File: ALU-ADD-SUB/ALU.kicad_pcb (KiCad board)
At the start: 4 copper layers, 122.2 x 30.8 mm, 26 parts, among them J1 Conn_01x02, J2 Conn_01x08, J3 Conn_01x08, J4 Conn_01x08, J5 Conn_01x02, J6 Conn_01x08, J8 Conn_01x02, U11 74LS245, U12 74LS283, U13 74LS283, U14 74LS86, U15 74LS86

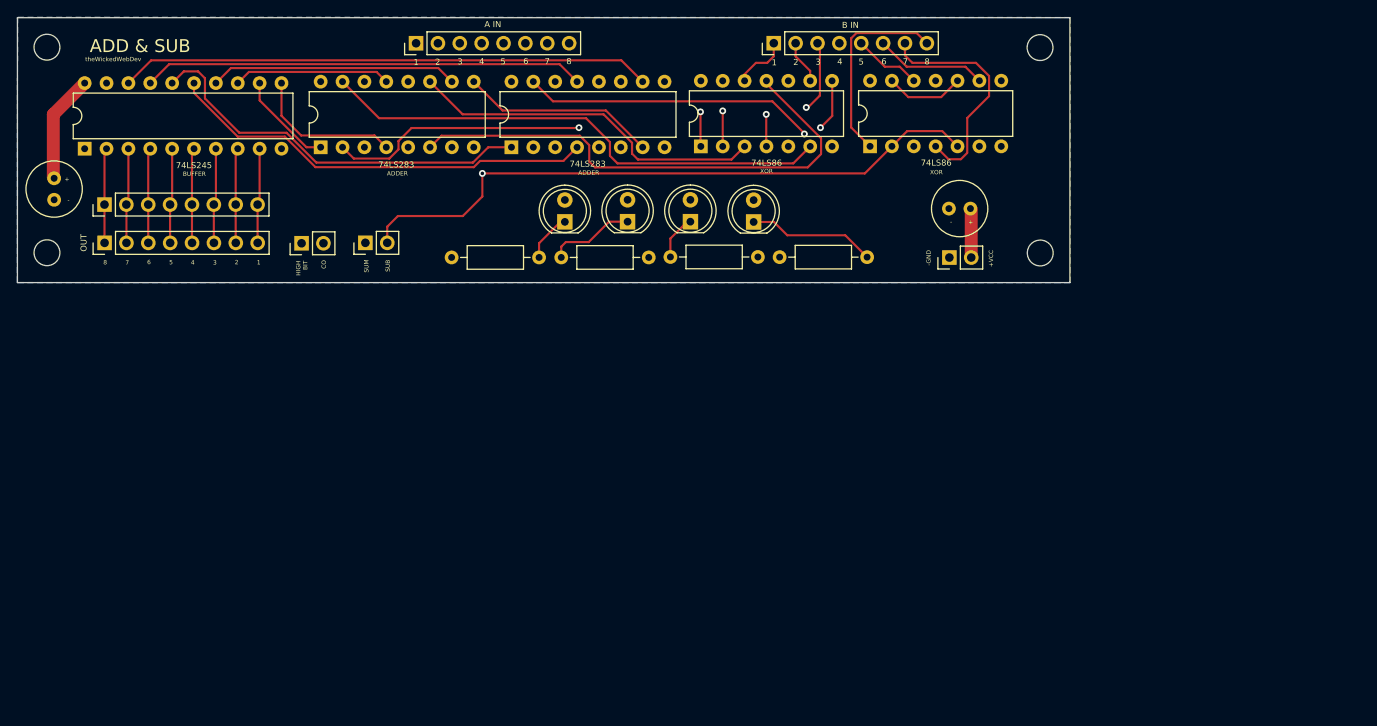
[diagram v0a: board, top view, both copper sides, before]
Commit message: Added Add/Sub Module
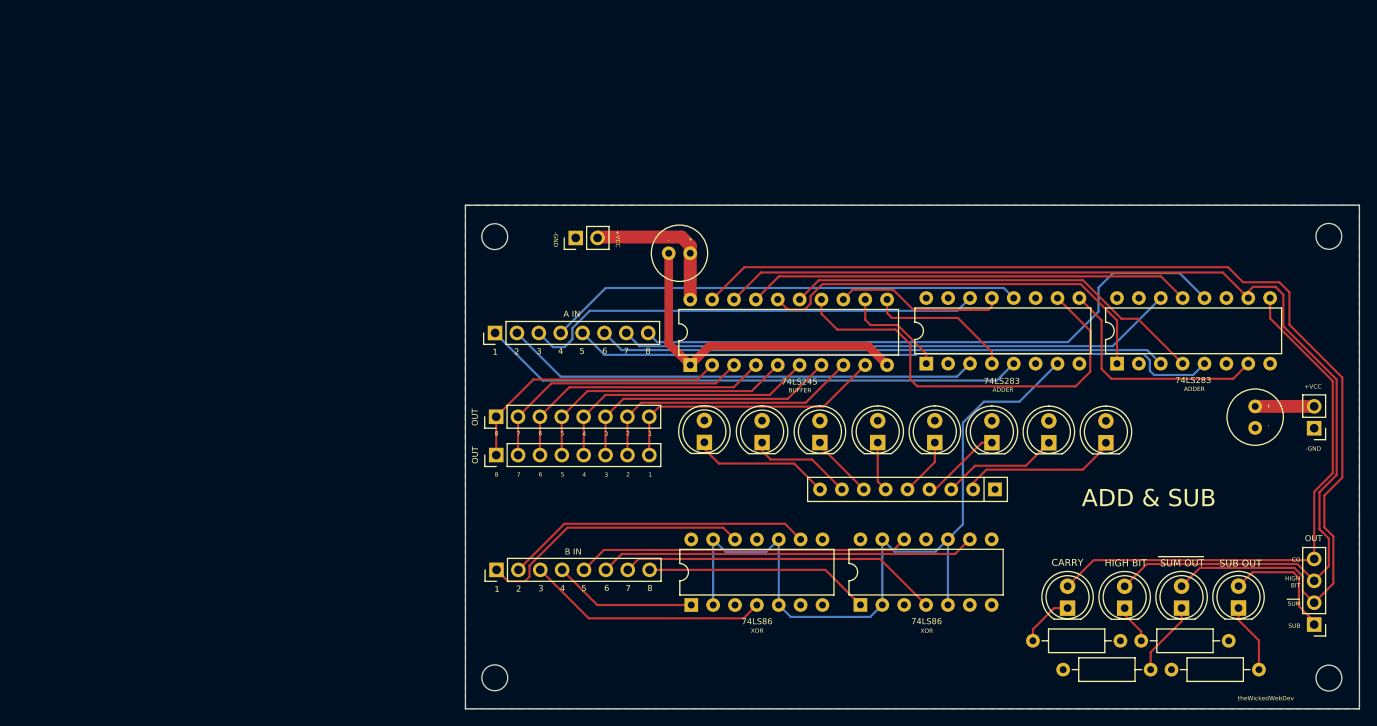
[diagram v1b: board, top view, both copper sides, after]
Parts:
- removed J8: Conn_01x02, Connector_PinHeader_2.54mm:PinHeader_1x02_P2.54mm_Vertical
- added D1: LED, LED_THT:LED_D5.0mm, F.Cu at (94.9, 80.8)
- added D2: LED, LED_THT:LED_D5.0mm, F.Cu at (101.6, 80.9)
- added D3: LED, LED_THT:LED_D5.0mm, F.Cu at (108.4, 80.9)
- added D4: LED, LED_THT:LED_D5.0mm, F.Cu at (115.1, 80.9)
- added D5: LED, LED_THT:LED_D5.0mm, F.Cu at (121.7, 80.9)
- added D6: LED, LED_THT:LED_D5.0mm, F.Cu at (128.3, 80.9)
- added D7: LED, LED_THT:LED_D5.0mm, F.Cu at (134.9, 80.9)
- added D8: LED, LED_THT:LED_D5.0mm, F.Cu at (141.6, 80.9)
- added J7: Conn_01x02, Connector_PinHeader_2.54mm:PinHeader_1x02_P2.54mm_Vertical, F.Cu at (80.0, 57.1)
- added RN1: R_Network08_US, Resistor_THT:R_Array_SIP9, F.Cu at (128.7, 86.3)
- J5: value Conn_01x02 -> Conn_01x04; footprint Connector_PinHeader_2.54mm:PinHeader_1x02_P2.54mm_Vertical -> Connector_PinHeader_2.54mm:PinHeader_1x04_P2.54mm_Vertical
- moved J5 118.8 mm to (165.8, 102.0), turned to 180 degrees
- moved R1 96.3 mm to (159.3, 107.2)
- moved D25 90.2 mm to (157.0, 100.1)
- moved R3 80.7 mm to (145.7, 103.9)
- moved U11 74.7 mm to (93.3, 71.9)
- moved U12 74.7 mm to (142.9, 71.7)
- moved U13 74.7 mm to (120.7, 71.7)
- moved C4 74.4 mm to (93.3, 58.9), turned to 180 degrees
- moved D27 73.1 mm to (143.7, 100.1)
- moved REF** 71.7 mm to (70.6, 108.2)
- moved J3 69.1 mm to (70.8, 95.7)
- moved D26 66.9 mm to (150.4, 100.1)
- moved D28 62.7 mm to (137.1, 100.1)
- moved R4 61.3 mm to (133.1, 103.9)
- moved REF** 59.7 mm to (167.5, 108.2)
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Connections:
- D25 pad 2: /SUM_OUT -> /SUB
- D26 pad 2: /SUB -> /SUM_OUT
- J5 pad 1: /SUM_OUT -> /SUB
- J5 pad 2: /SUB -> /SUM_OUT
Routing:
- net VCC: track 149.1 -> 24.3 mm
- net A8: track 6.58 -> 71.2 mm
- net A7: track 4.84 -> 65.0 mm
- net /SUM_OUT: track 71.3 -> 130.2 mm
- net A5: track 22.5 -> 75.6 mm
- net A6: track 13.5 -> 66.1 mm
- net A4: track 10.9 -> 55.3 mm
- net /SUM4: track 28.8 -> 71.1 mm
- net A3: track 12.9 -> 53.9 mm
- net Net-(U12-Pad11): track 37.1 -> 77.1 mm
- net GND: track 0.00 -> 38.7 mm
- net Net-(U13-Pad11): track 41.6 -> 78.4 mm
- net A2: track 20.1 -> 56.1 mm
- net /SUM1: track 17.5 -> 52.9 mm
- net /SUM8: track 110.8 -> 145.2 mm
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- added copper zone on In2.Cu, net VCC
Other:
- board size 122.2 x 30.8 mm -> 103.8 x 58.5 mm
- board text added: "CARRY"
- board text added: "SUB OUT"
- board text added: "SUM OUT"

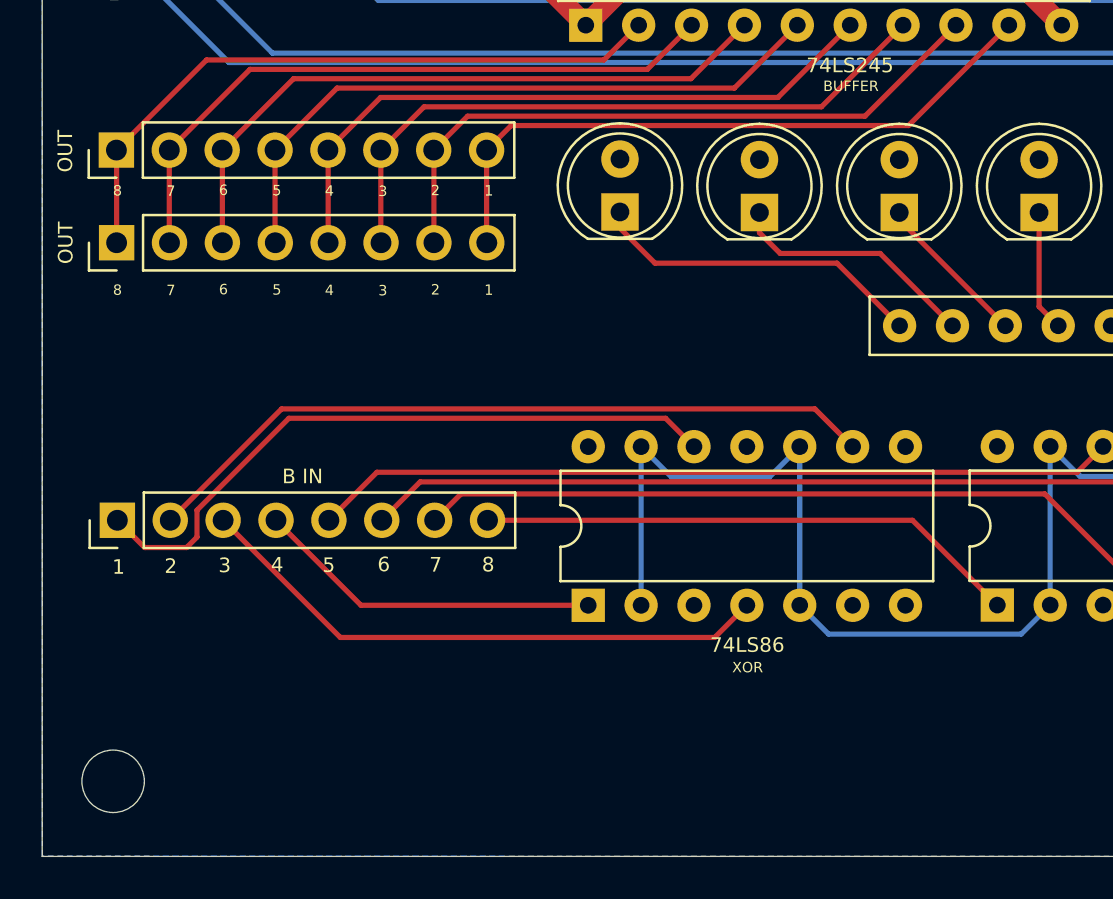
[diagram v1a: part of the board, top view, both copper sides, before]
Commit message: BiDirectional Shift Register component
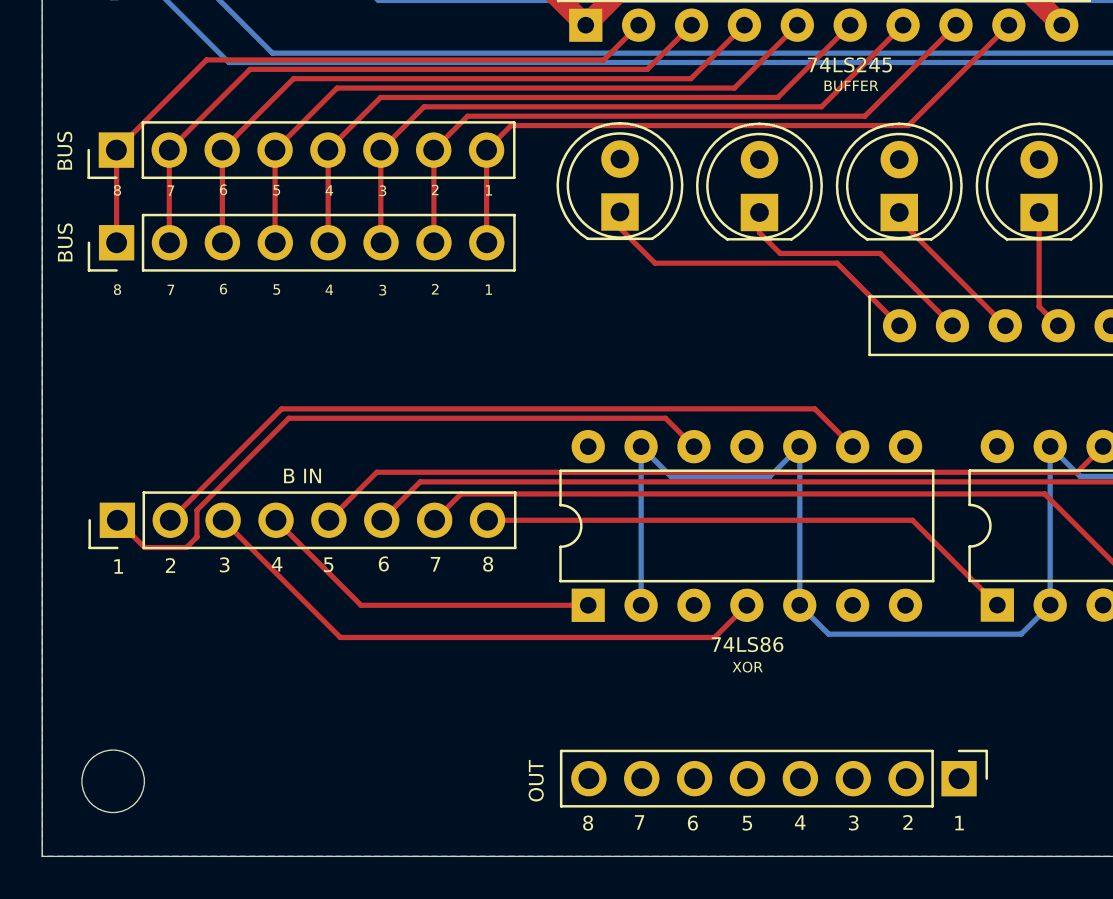
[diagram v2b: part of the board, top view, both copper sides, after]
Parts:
- added J8: Conn_01x08, Connector_PinHeader_2.54mm:PinHeader_1x08_P2.54mm_Vertical, F.Cu at (111.2, 108.1)
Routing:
- net /SUM1: track 52.9 -> 139.3 mm
- net /SUM2: track 42.9 -> 121.3 mm
- net /SUM3: track 45.7 -> 116.0 mm
- net /SUM4: track 71.1 -> 133.4 mm
- net /SUM5: track 68.3 -> 122.6 mm
- net /SUM6: track 64.5 -> 110.7 mm
- net /SUM7: track 67.0 -> 107.1 mm
- net /SUM8: track 145.2 -> 182.6 mm
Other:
- board text added: "BUS"

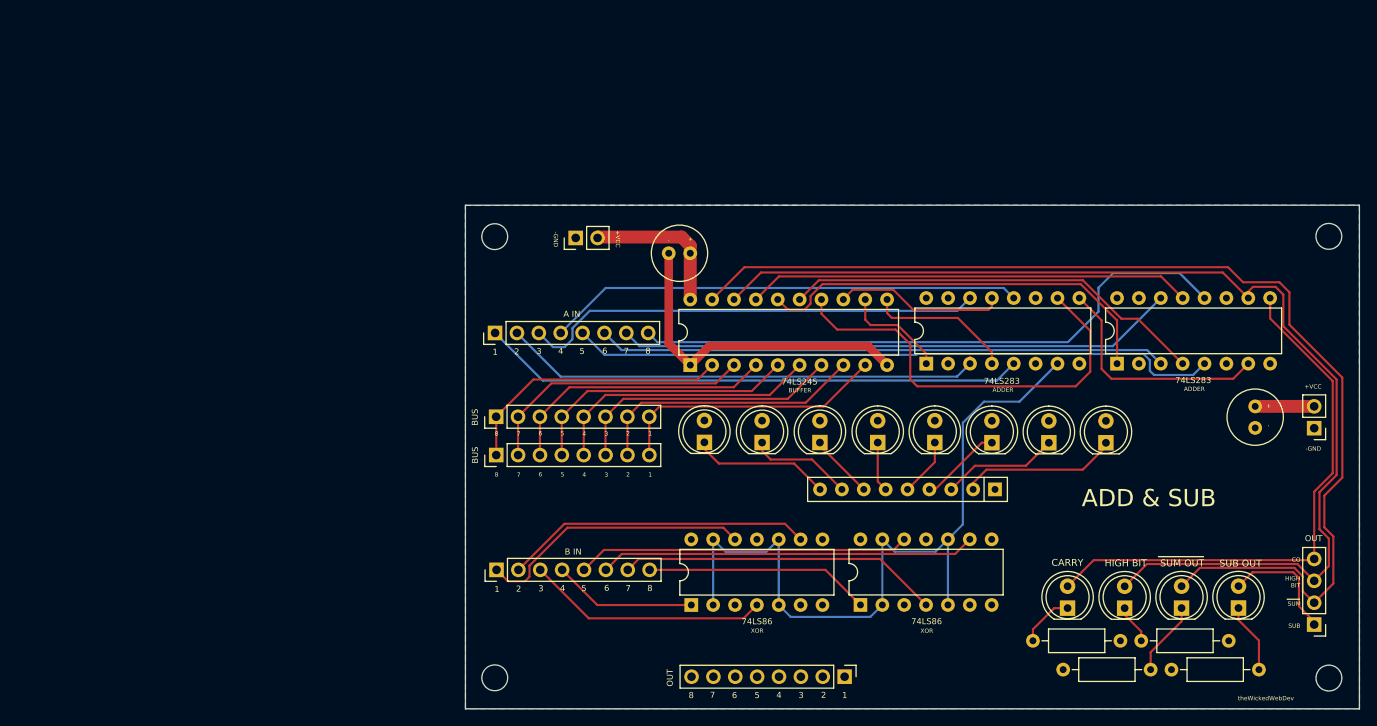
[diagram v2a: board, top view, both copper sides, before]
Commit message: Updated ADD/SUB module
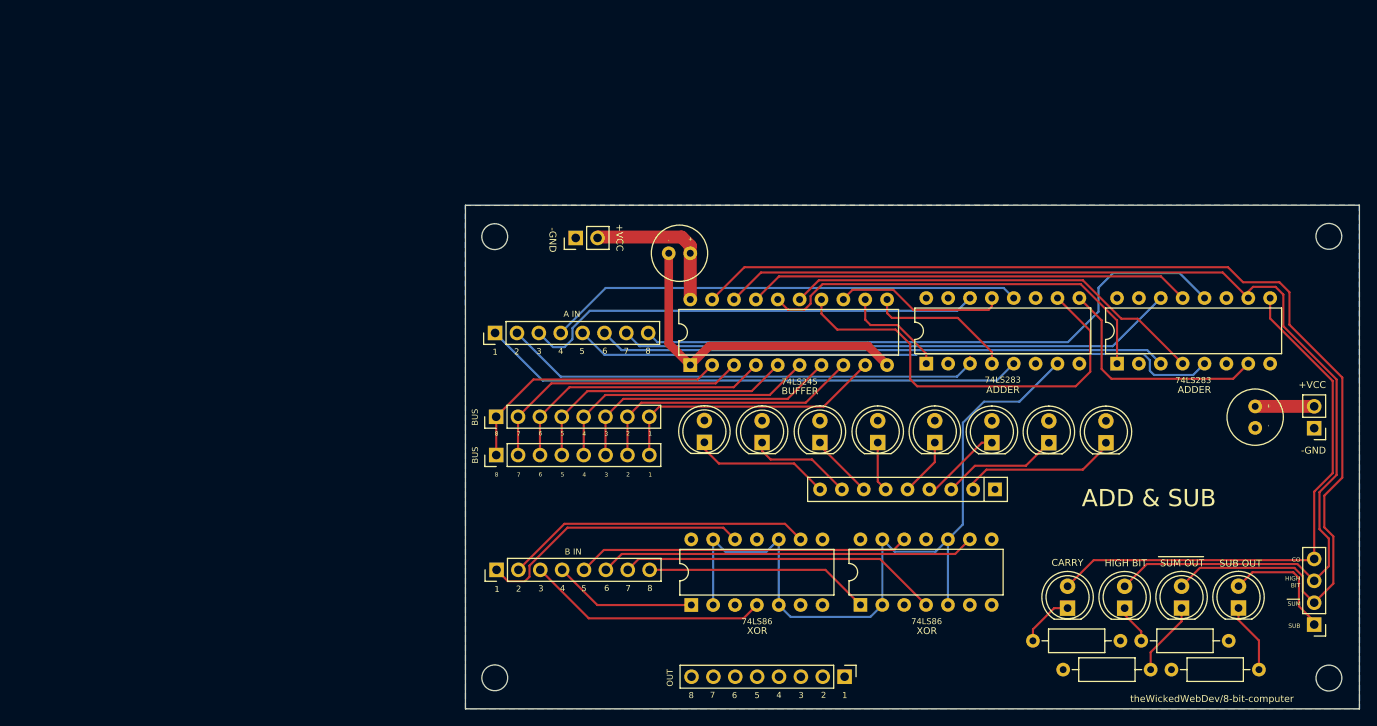
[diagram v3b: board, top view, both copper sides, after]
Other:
- board text added: "theWickedWebDev/8-bit-computer"
- board text removed: "theWickedWebDev"
